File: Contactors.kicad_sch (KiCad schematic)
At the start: 9 parts, among them J10 A_PRCHG_BYPASS, J11 M_PRCHG_BYPASS, J17 M_CNTCTR, U10 EL3H7, U8 EL3H7, U9 EL3H7

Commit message: Added version update notes.
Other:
- note added: "- Separated contactors to 1 per connector - Added sense pins - Removed array contactor"
- note removed: "Added Motor_Contactor"
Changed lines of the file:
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@@
 		)
 	)
-	(text "Added Motor_Contactor"
+	(text "- Separated contactors to 1 per connector\n- Added sense pins\n- Removed array contactor"
 		(exclude_from_sim no)
 		(at 178.054 180.086 0)

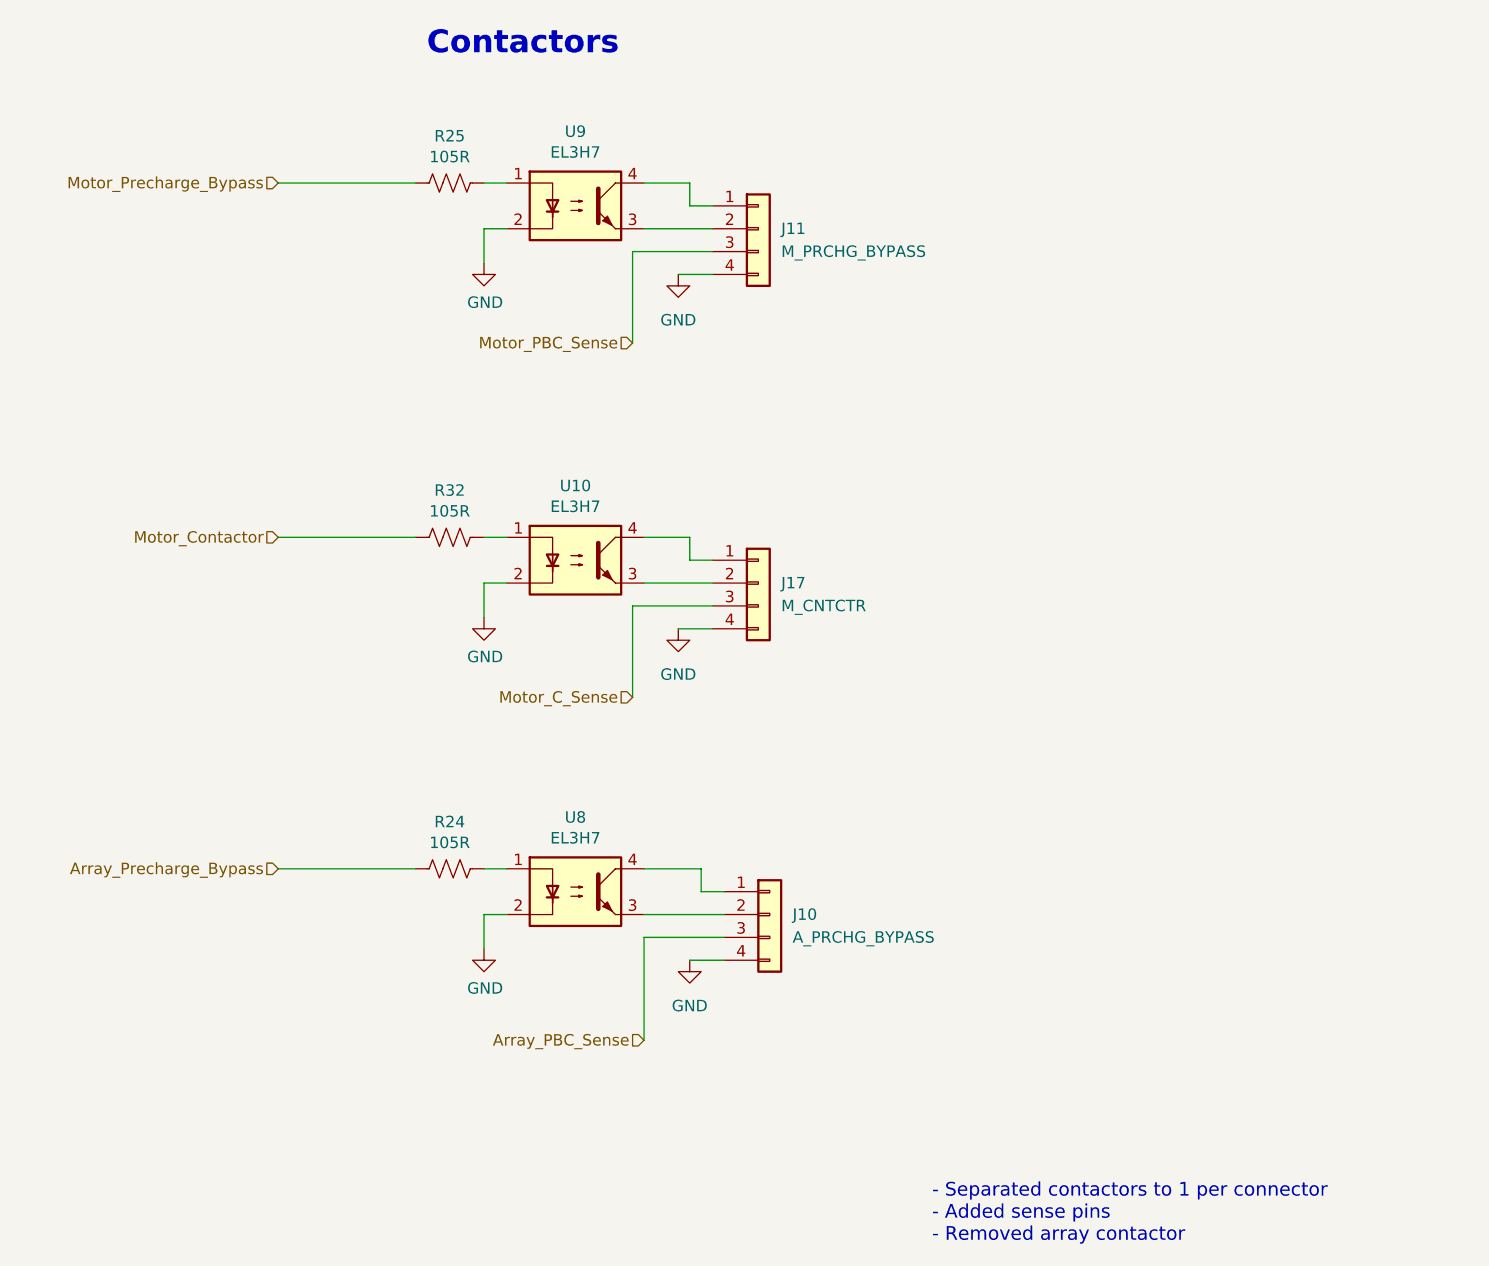
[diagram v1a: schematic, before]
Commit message: Added pullup resistors to schematic.
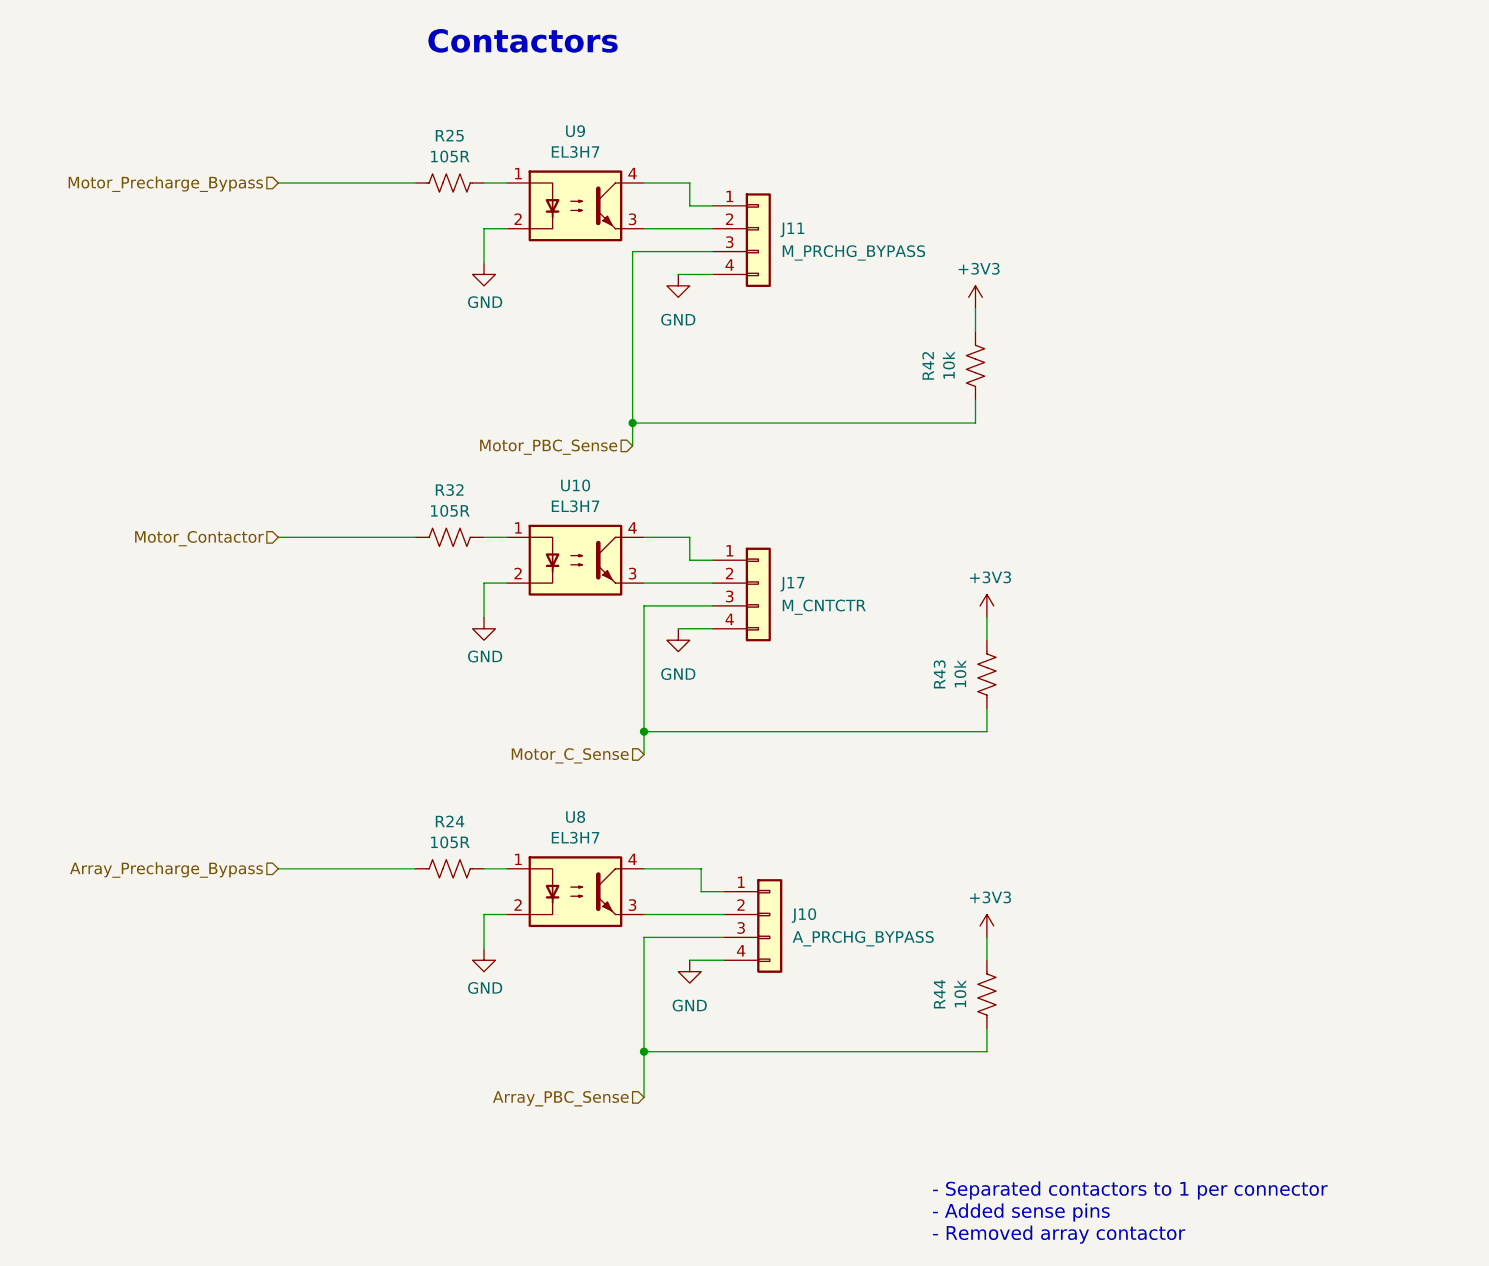
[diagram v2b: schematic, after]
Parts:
- added R42, R43, R44: 10k, Resistor_SMD:R_0805_2012Metric, symbol Device:R_US
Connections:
- net Array_PBC_Sense: now also R44.2
- net Motor_C_Sense: now also R43.2
- net Motor_PBC_Sense: now also R42.2
- new net +3V3: R42.1, R43.1, R44.1

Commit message: Added pullup resistors to layout; changed the 105R to just 105 on the contactors page because I think that's what it was supposed to be.
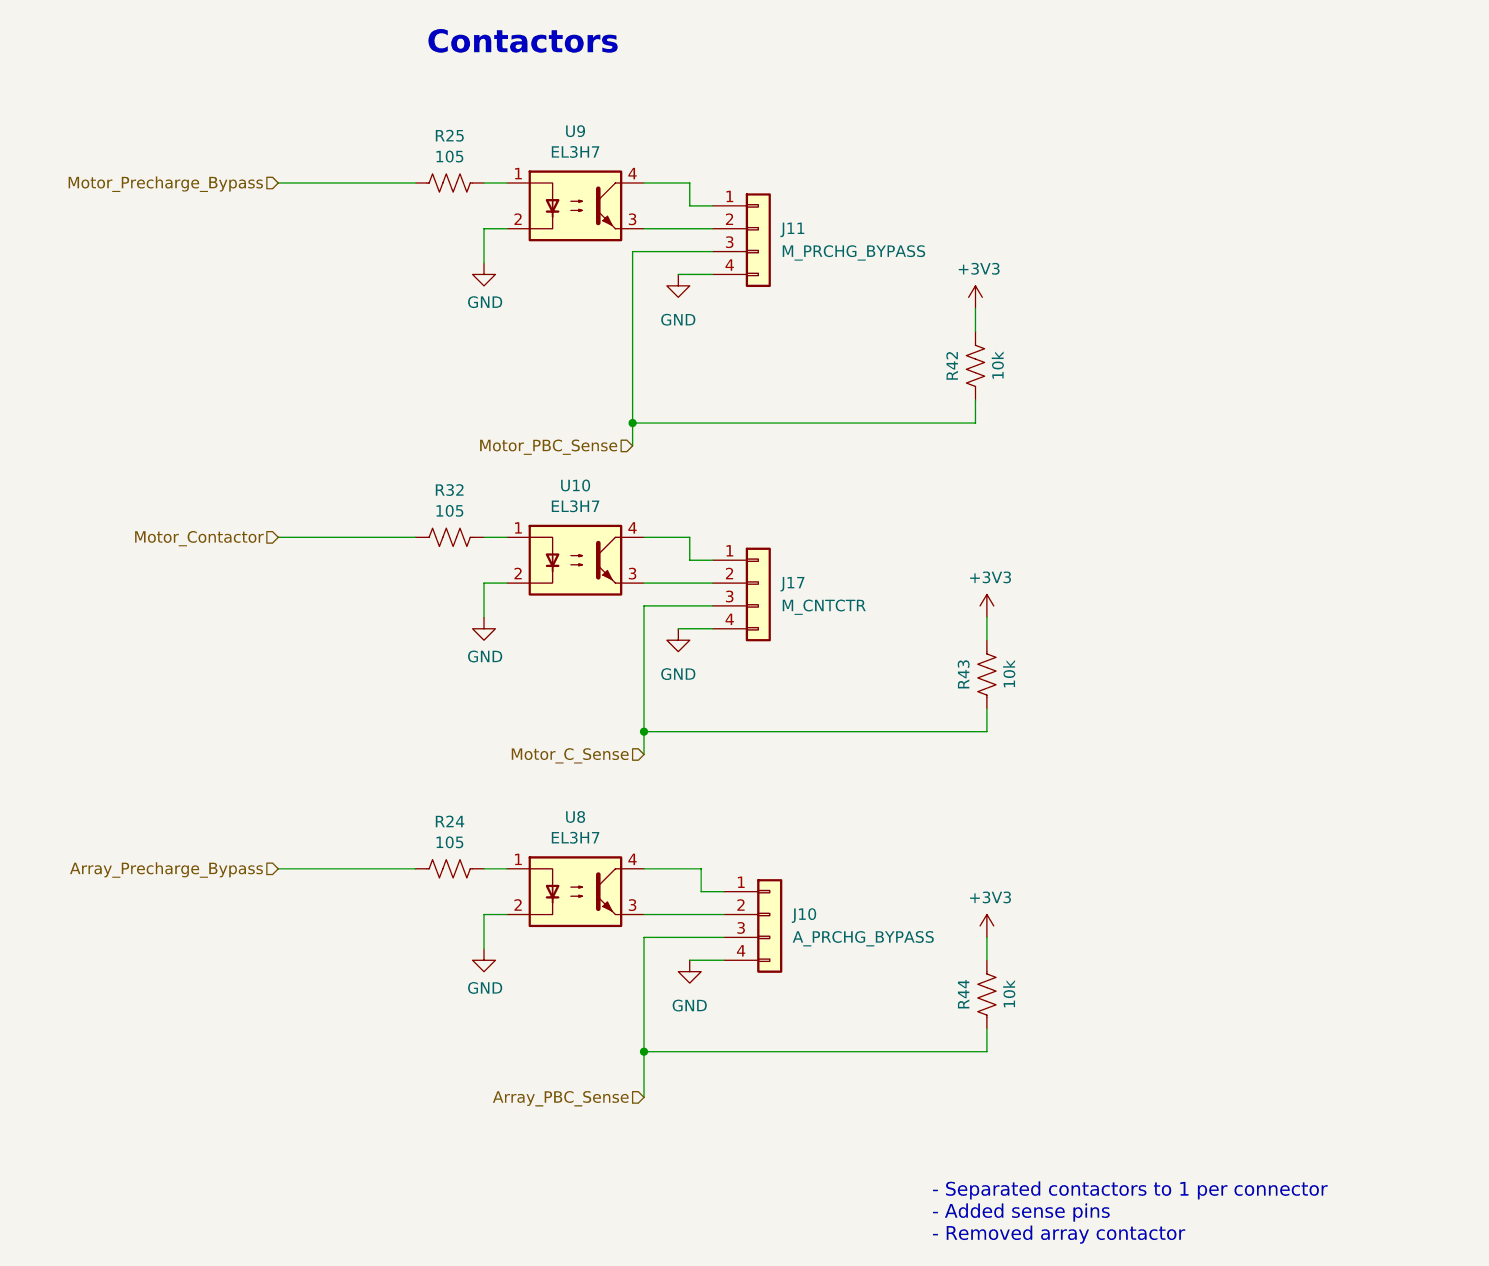
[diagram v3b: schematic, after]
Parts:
- R24, R25, R32: value 105R -> 105
- R42, R43, R44: Mouser Part Number 71-CRCW0805105RFKEA -> 71-CRCW080510K0FKEAC; P/N CRCW0805105RFKEA -> CRCW080510K0FKEAC

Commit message: Removed precharge contactor stuff, made accel 5V instead of 3, removed op amp for brake.
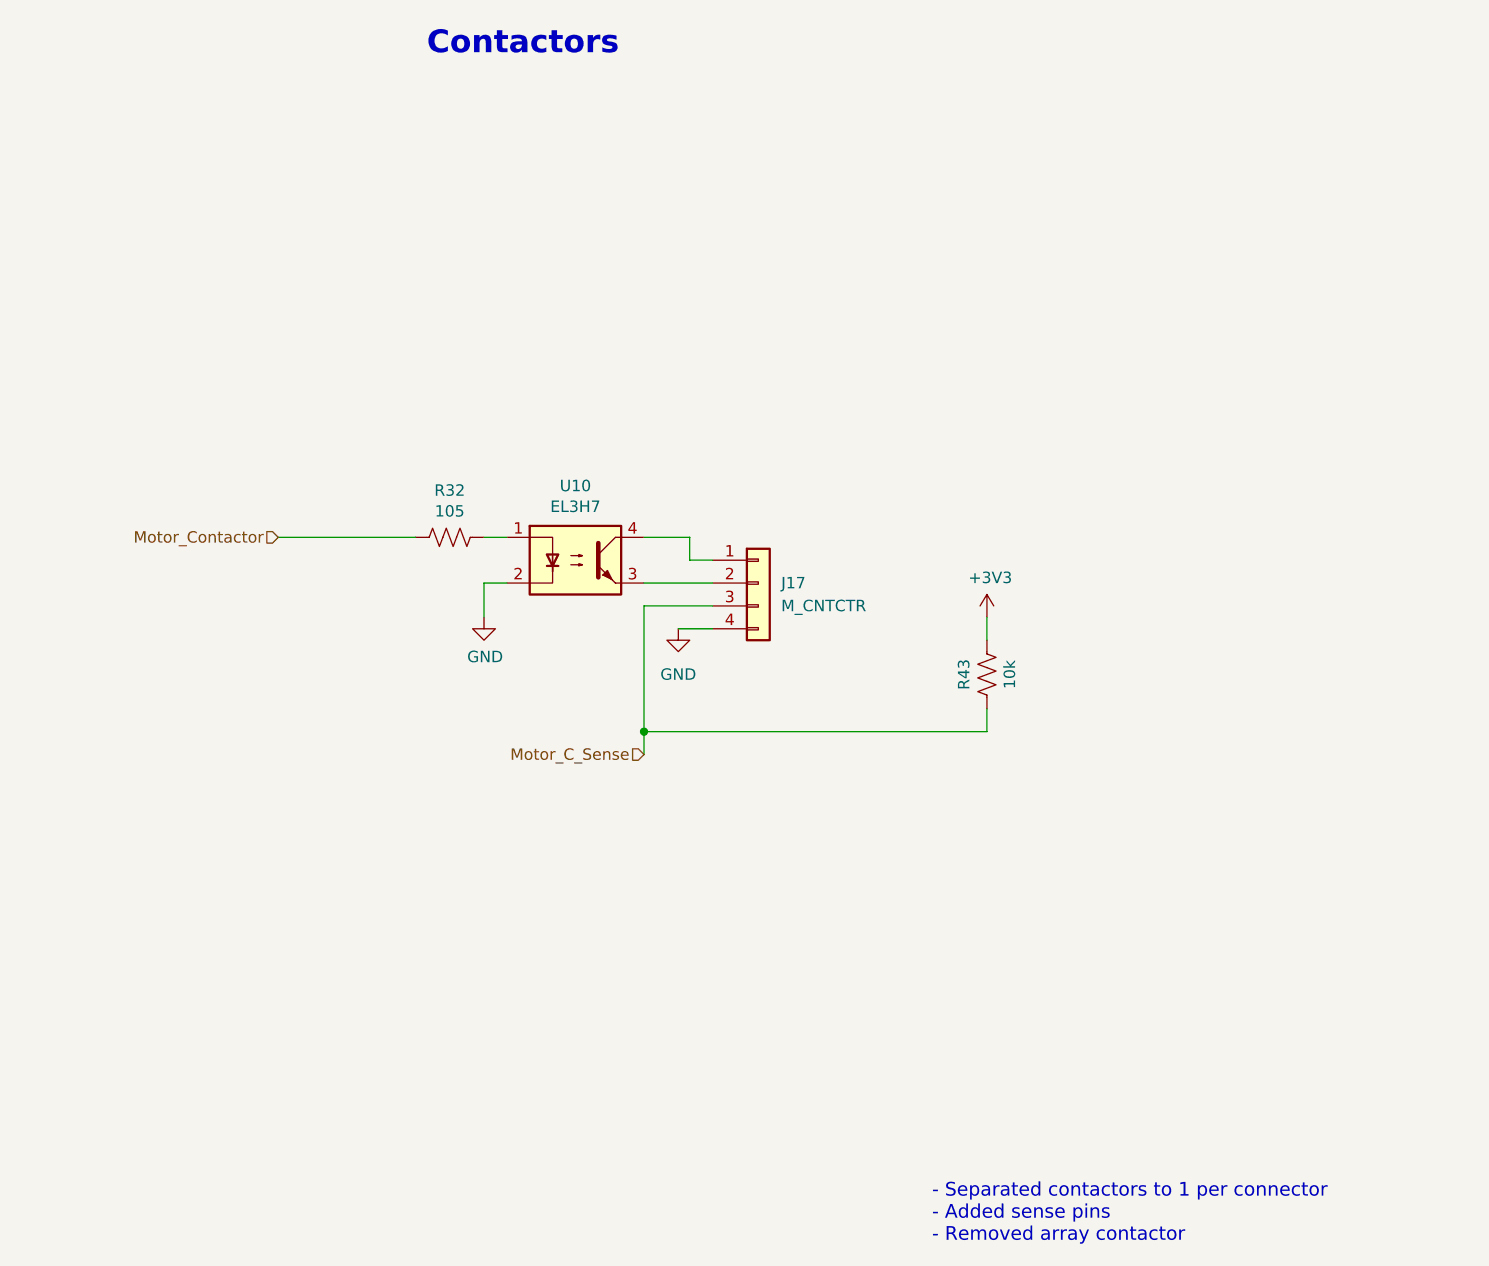
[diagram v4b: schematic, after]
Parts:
- removed J10: A_PRCHG_BYPASS, Connector_Molex:Molex_Micro-Fit_3.0_43650-0415_1x04_P3.00mm_Vertical, symbol Connector_Generic:Conn_01x04
- removed J11: M_PRCHG_BYPASS, Connector_Molex:Molex_Micro-Fit_3.0_43650-0415_1x04_P3.00mm_Vertical, symbol Connector_Generic:Conn_01x04
- removed R24, R25: 105, Resistor_SMD:R_0805_2012Metric, symbol Device:R_US
- removed R42, R44: 10k, Resistor_SMD:R_0805_2012Metric, symbol Device:R_US
- removed U8, U9: EL3H7, Package_SO:SSOP-4_4.4x2.6mm_P1.27mm, symbol Isolator:SFH617A-1

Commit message: Added part numbers wheeeeeeeeeeeeeeeeeeeee
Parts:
- R32: JLCPCB# (none) -> C17437
- R43: JLCPCB# (none) -> C17414
- U10: JLCPCB# (none) -> C32565
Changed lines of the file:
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@@
+			)
+		)
+		(property "JLCPCB#" "C17437"
+			(at 124.46 101.6 0)
+			(effects
+				(font
+					(size 1.27 1.27)
+				)
+				(hide yes)
 			)
 		)
@@
 			)
 		)
+		(property "JLCPCB#" ""
+			(at 158.75 106.68 0)
+			(effects
+				(font
+					(size 1.27 1.27)
+				)
+				(hide yes)
+			)
+		)
 		(pin "1"
 		)
@@
 			)
 		)
+		(property "JLCPCB#" "C32565"
+			(at 138.43 104.14 0)
+			(effects
+				(font
+					(size 1.27 1.27)
+				)
+				(hide yes)
+			)
+		)
 		(pin "1"
 		)
@@
 			(at 184.15 116.84 0)
 			(effects
+				(font
+					(size 1.27 1.27)
+				)
+				(hide yes)
+			)
+		)
+		(property "JLCPCB#" "C17414"
+			(at 184.15 116.84 0)
+			(effects

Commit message: Change schottky diode footprint, update JLCPcB parts.
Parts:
- U10: JLCPCB# C32565 -> C92243
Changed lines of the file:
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@@
 			)
 		)
-		(property "JLCPCB#" "C32565"
+		(property "JLCPCB#" "C92243"
 			(at 138.43 104.14 0)
 			(effects
